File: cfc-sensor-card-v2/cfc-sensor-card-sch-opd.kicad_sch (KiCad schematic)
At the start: 73 parts, among them Q1 DMP2240UDM, Q2 PMV45EN, Q3 DMP3050LVT-7, Q4 DMP3050LVT-7, Q5 PMV45EN, U2 MAX7310, U3 MIC842LYC5, U4 MIC842LYC5, U5 MAX4211FETE

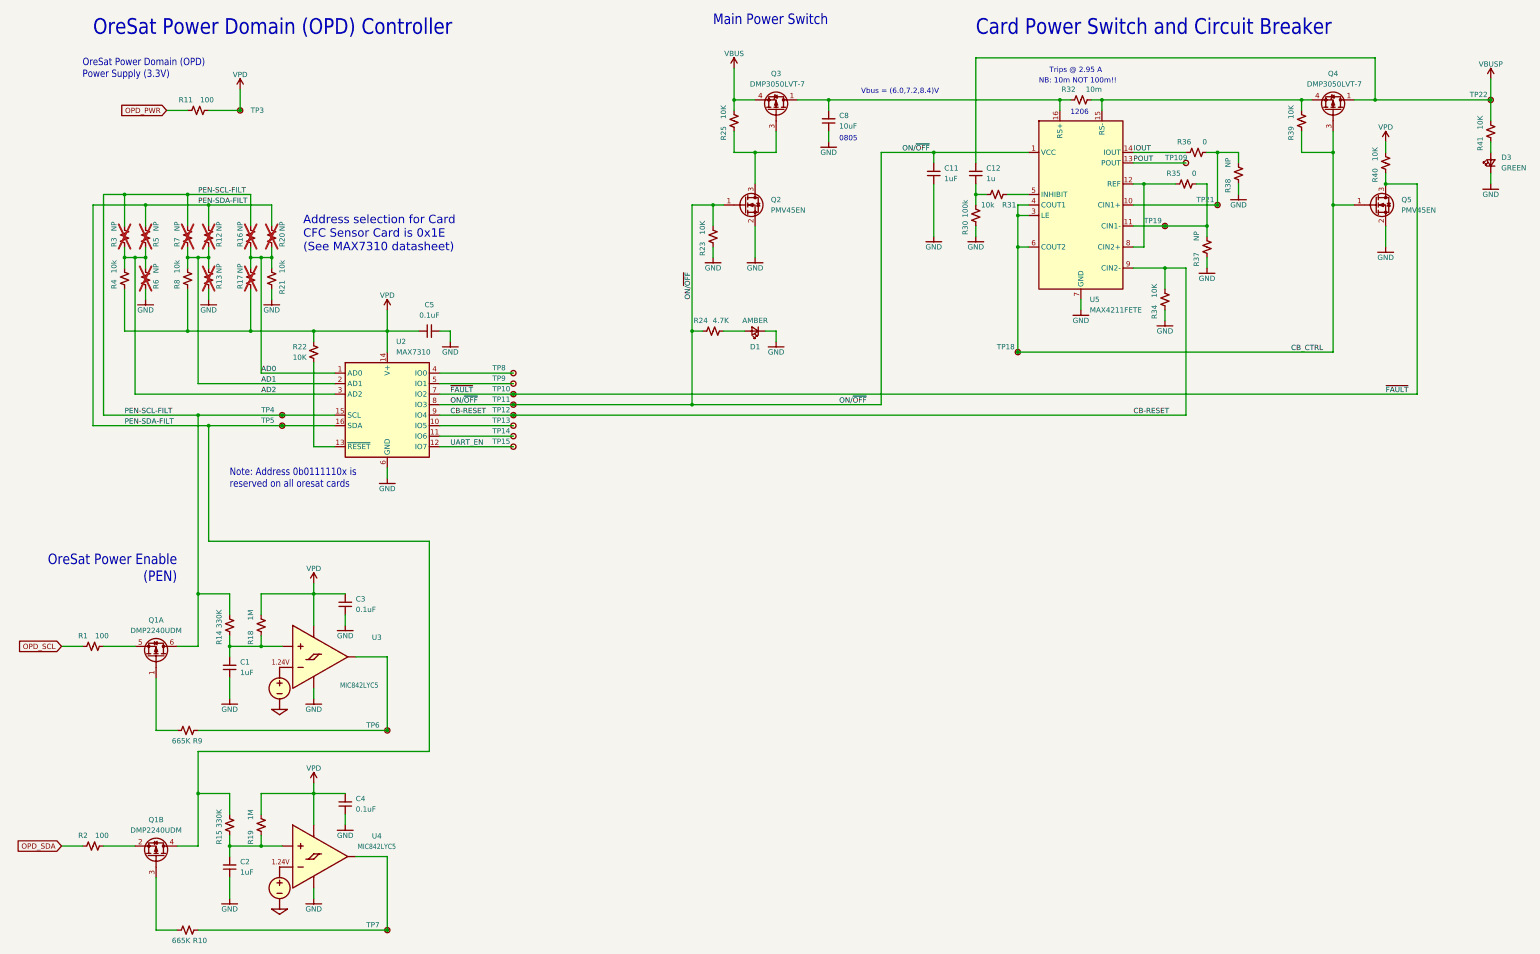
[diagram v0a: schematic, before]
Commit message: Fix and complete BOM, fix lots of little layout issue and footprint inconsistancies, and polish. Ready to go!
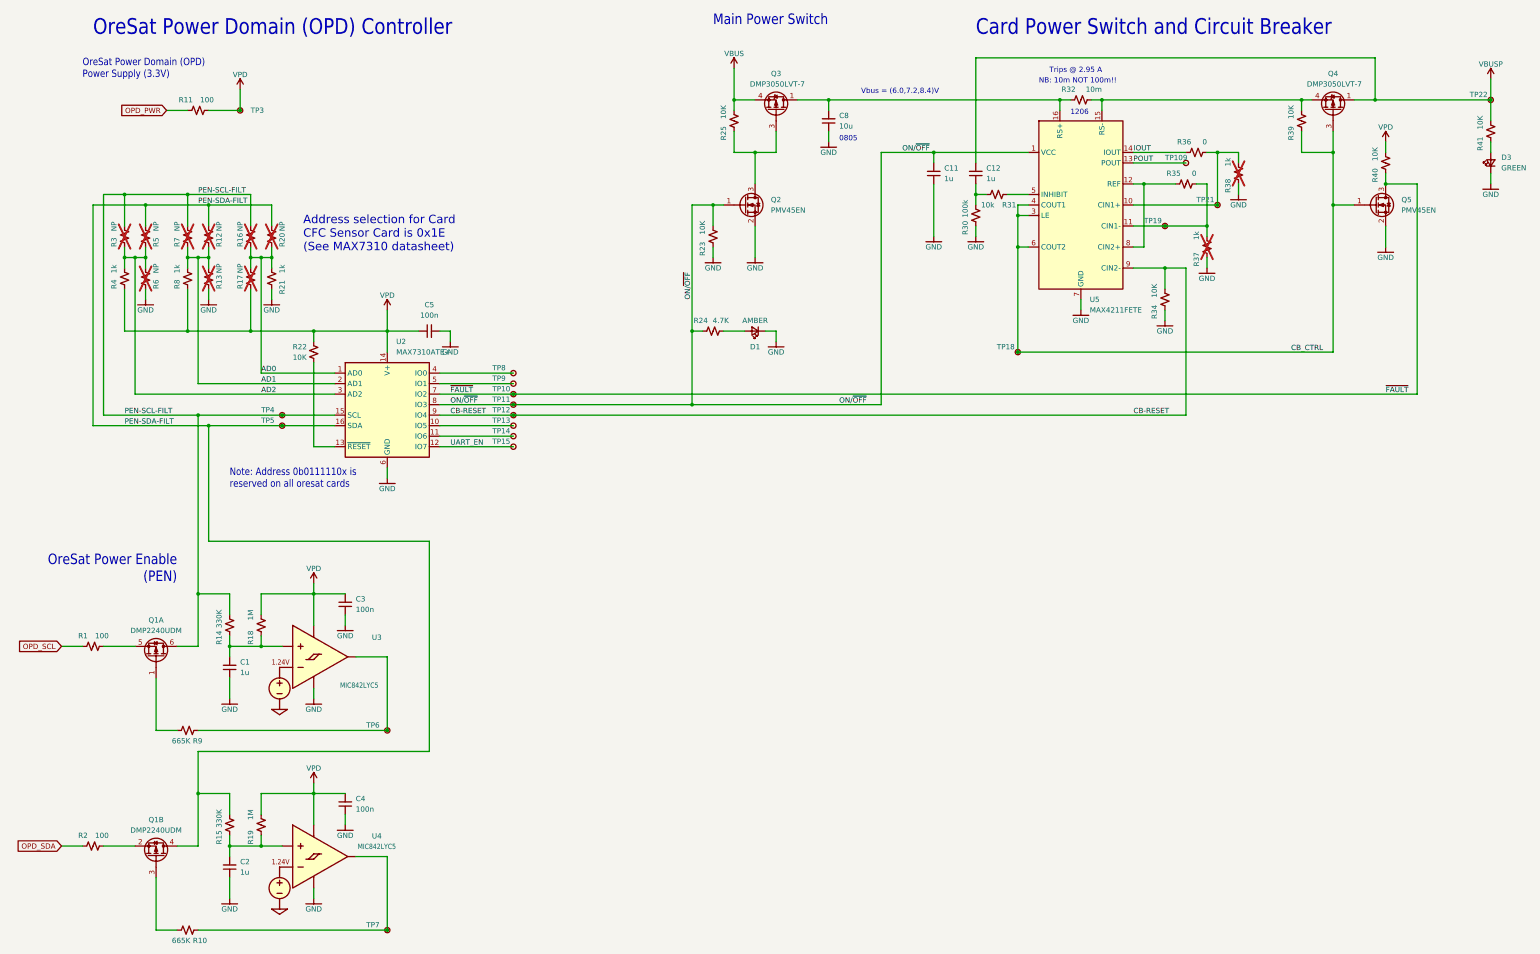
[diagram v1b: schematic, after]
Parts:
- C1, C11, C2: value 1uF -> 1u; DIS (none) -> DigiKey; DPN (none) -> 587-3473-1-ND; MFR (none) -> Taiyo Yuden; MPN (none) -> TMK107BJ105KAHT
- C12: DIS (none) -> DigiKey; DPN (none) -> 587-3473-1-ND; MFR (none) -> Taiyo Yuden; MPN (none) -> TMK107BJ105KAHT
- C3, C4, C5: value 0.1uF -> 100n; DIS (none) -> DigiKey; DPN (none) -> 587-3472-1-ND; MFR (none) -> Taiyo Yuden; MPN (none) -> TMK107BJ104KAHT
- C8: value 10uF -> 10u; DIS (none) -> DigiKey; DPN (none) -> 490-GRT21BC71E106KE13LCT-ND; MFR (none) -> Murata Electronics; MPN (none) -> GRT21BC71E106KE13L
- D1: DIS (none) -> DigiKey; DPN (none) -> 732-150060AS75000CT-ND; MFR (none) -> Wurth; MPN (none) -> 150060AS75000
- D3: DIS (none) -> DigiKey; DPN (none) -> 732-4971-1-ND; MFR (none) -> Wurth; MPN (none) -> 150060GS75000
- Q1: footprint Package_TO_SOT_SMD:SOT-23-6_Handsoldering -> Package_TO_SOT_SMD:SOT-23-6; DIS (none) -> DigiKey; DPN (none) -> DMP2240UDMDICT-ND; MFR (none) -> Diodes Inc; MPN (none) -> DMP2240UDM
- Q2, Q5: DIS (none) -> DigiKey; DPN (none) -> 1727-2307-1-ND; MFR (none) -> Nexperia; MPN (none) -> PMV45EN2R
- Q3, Q4: DIS (none) -> DigiKey; DPN (none) -> DMP3050LVT-7DICT-ND; MFR (none) -> Diodes Inc; MPN (none) -> DMP3050LVT-7
- R1, R11, R2: DIS (none) -> DigiKey; DPN (none) -> RMCF0603FT100RCT-ND; MFR (none) -> Stackpole Electronics Inc; MPN (none) -> RMCF0603FT100R
- R10, R9: DIS (none) -> DigiKey; DPN (none) -> RMCF0603FT665KCT-ND; MFR (none) -> Stackpole Electronics Inc; MPN (none) -> RMCF0603FT665K
- R14, R15: DIS (none) -> DigiKey; DPN (none) -> RMCF0603FT330KCT-ND; MFR (none) -> Stackpole Electronics Inc; MPN (none) -> RMCF0603FT330K
- R18, R19: DIS (none) -> DigiKey; DPN (none) -> RMCF0603FG1M00CT-ND; MFR (none) -> Stackpole Electronics Inc; MPN (none) -> RMCF0603FG1M00
- R21, R4, R8: value 10k -> 1k; DIS (none) -> DigiKey; DPN (none) -> RMCF0603FT1K00CT-ND; MFR (none) -> Stackpole Electronics Inc; MPN (none) -> RMCF0603FT1K00
- R22, R23, R25, R31, R34, R39, R40, R41: DIS (none) -> DigiKey; DPN (none) -> RMCF0603FT10K0CT-ND; MFR (none) -> Stackpole Electronics Inc; MPN (none) -> RMCF0603FT10K0
- R24: DIS (none) -> DigiKey; DPN (none) -> RMCF0603FT4K70CT-ND; MFR (none) -> Stackpole Electronics Inc; MPN (none) -> RMCF0603FT4K70
- R30: DIS (none) -> DigiKey; DPN (none) -> RMCF0603FT100KCT-ND; MFR (none) -> Stackpole Electronics Inc; MPN (none) -> RMCF0603FT100K
- R32: DIS (none) -> DigiKey; DPN (none) -> CSRF1206FT10L0CT-ND; MFR (none) -> Stackpole Electronics Inc; MPN (none) -> CSRF1206FT10L0
- R35, R36: DIS (none) -> DigiKey; DPN (none) -> RMCF0603ZT0R00CT-ND; MFR (none) -> Stackpole Electronics Inc; MPN (none) -> RMCF0603ZT0R00
- R37, R38: value NP -> 1k; now not fitted
- TP10, TP109, TP11, TP12, TP13, TP14, TP15, TP18, TP19, TP21, TP22, TP3, TP4, TP5, TP6, TP7, TP8, TP9: footprint oresat-misc:TestPoint-0.75mm-th -> oresat-misc:TestPoint-MinTH; now left out of the parts list
- U2: value MAX7310 -> MAX7310ATE+; DIS (none) -> DigiKey; DPN (none) -> MAX7310ATE+-ND; MFR (none) -> Analog Devices; MPN (none) -> MAX7310ATE+
- U3, U4: DIS (none) -> DigiKey; DPN (none) -> 576-2927-1-ND; MFR (none) -> Microchip Technology; MPN (none) -> MIC842LYC5-TR
- U5: DIS (none) -> DigiKey; DPN (none) -> MAX4211FETE+-ND; MFR (none) -> Analog Devices; MPN (none) -> MAX4211FETE
